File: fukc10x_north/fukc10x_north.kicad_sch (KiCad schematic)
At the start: 50 parts, among them J1 SM04B-SRSS-TB, J2 LED_Conn01x02_Pin, J3 LED_Conn01x02_Pin, J4 LED_Conn01x02_Pin, J5 LED_Conn01x02_Pin, J6 LED_Conn01x02_Pin, J7 LED, J8 LED_Conn01x02_Pin, Q1 AO3401A, Q2 2N7002, Q3 2N7002, Q4 2N7002, Q5 2N7002, U1 XC6206P332MR, U2 STM32F072CBT6

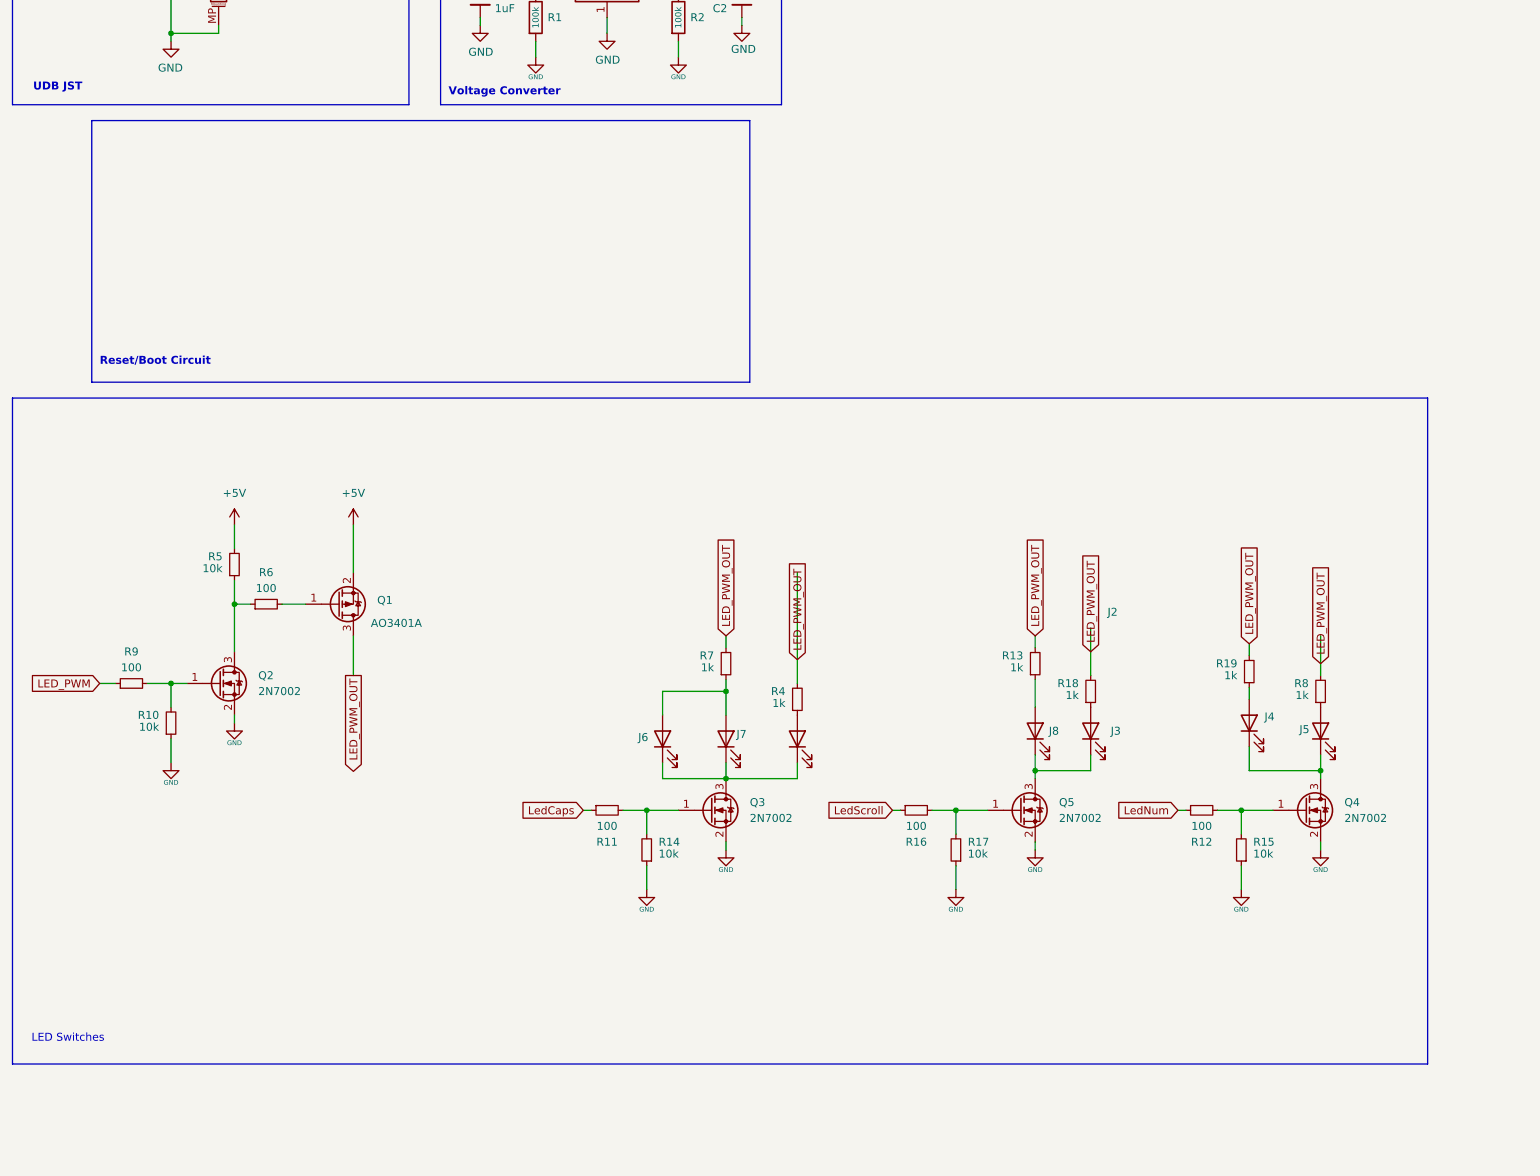
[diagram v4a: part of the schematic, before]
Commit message: adjusted some traces, flipped some switches, went through drc again
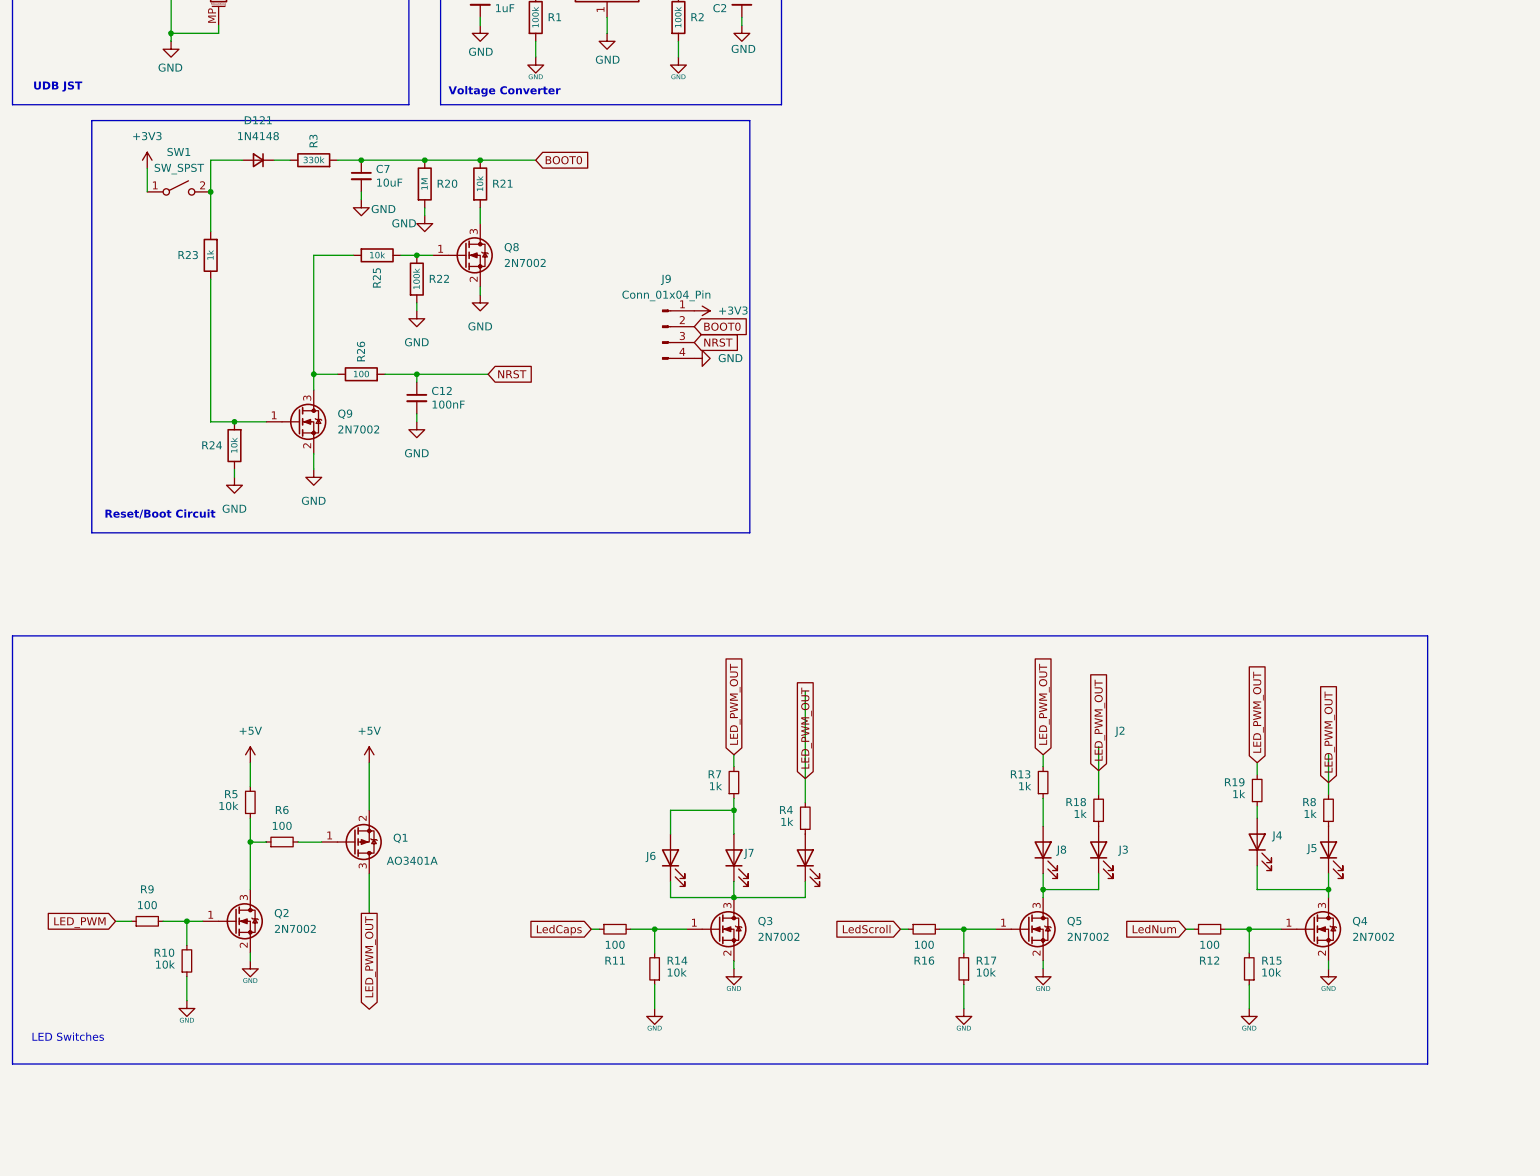
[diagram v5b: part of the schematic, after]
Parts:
- added C12: 100nF, Capacitor_SMD:C_0402_1005Metric, symbol Device:C_Small
- added C7: 10uF, Capacitor_SMD:C_0402_1005Metric, symbol Device:C_Small
- added D121: 1N4148, Diode_SMD:D_SOD-123, symbol Device:D_Small
- added J9: Conn_01x04_Pin, acheron_Connectors:PinHeader_1x4_P2.54mm_Vertical, symbol Connector:Conn_01x04_Pin
- added Q8, Q9: 2N7002, Package_TO_SOT_SMD:SOT-23, symbol Transistor_FET:2N7002
- added R20: 1M, Resistor_SMD:R_0402_1005Metric, symbol Device:R
- added R21, R24, R25: 10k, Resistor_SMD:R_0402_1005Metric, symbol Device:R
- added R22: 100k, Resistor_SMD:R_0402_1005Metric, symbol Device:R
- added R23: 1k, Resistor_SMD:R_0402_1005Metric, symbol Device:R
- added R26: 100, Resistor_SMD:R_0402_1005Metric, symbol Device:R
- added R3: 330k, Resistor_SMD:R_0402_1005Metric, symbol Device:R
- added SW1: SW_SPST, Button_Switch_SMD:SW_SPST_TL3342, symbol Switch:SW_SPST
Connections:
- net +3V3: now also J9.1 (Pin_1), SW1.1 (A)
- net BOOT0: now also C7.1, J9.2 (Pin_2), R20.1, R21.1, R3.2
- net GND: now also C12.2, C7.2, J9.4 (Pin_4), Q8.2 (S), Q9.2 (S), R20.2, R22.2, R24.1
- net NRST: now also C12.1, J9.3 (Pin_3), R26.2
- new net: D121.1 (K), R3.1
- new net: D121.2 (A), R23.2, SW1.2 (B)
- new net: Q9.1 (G), R23.1, R24.2
- new net: Q8.1 (G), R22.1, R25.1
- new net: Q8.3 (D), R21.2
- new net: Q9.3 (D), R25.2, R26.1
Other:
- moved on the sheet: J2, J3, J4, J5, J6, J7, J8, Q1, Q2, Q3, Q4, Q5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
